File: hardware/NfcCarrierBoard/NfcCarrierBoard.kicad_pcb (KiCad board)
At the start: 2 copper layers, 80 x 100 mm, 50 parts, among them J1 Barrel_Jack, J2 Conn_01x03, J3 JST SH 4, J4 Grove, J5 Conn_01x03, J6 UART, J7 Grove UART, Q1 NMOS, Q2 NMOS, SW1 RESET, U1 24AA02E-OT

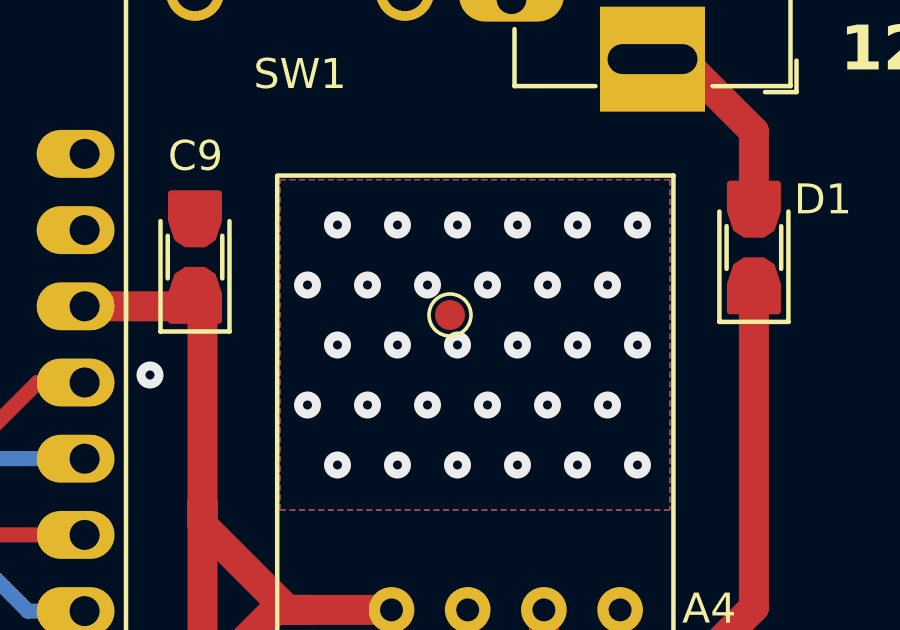
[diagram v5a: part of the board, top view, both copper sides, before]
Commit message: Adjust silkscreen Expose heatsink pad
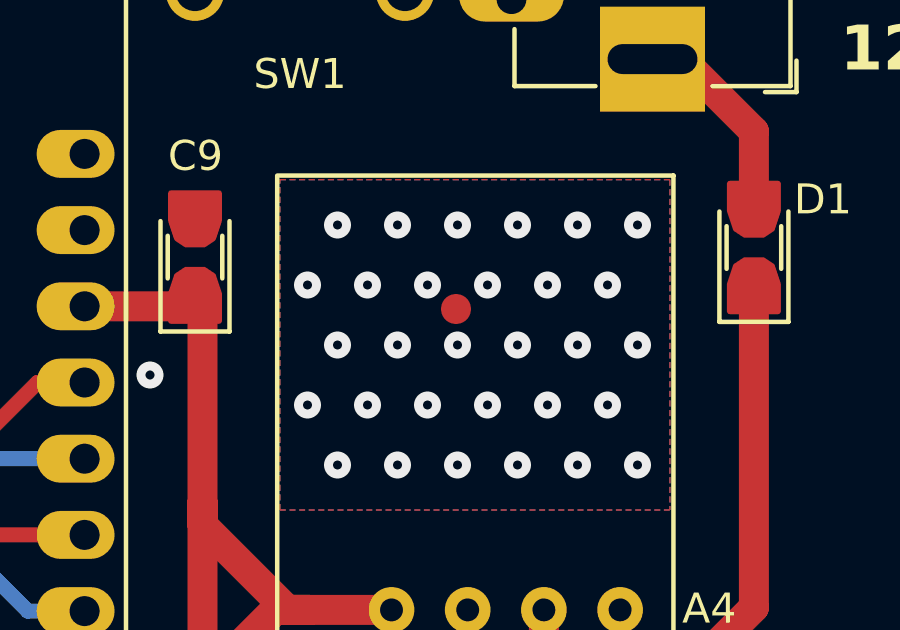
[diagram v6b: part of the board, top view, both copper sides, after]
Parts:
- moved SYM1 2.00 mm to (140.0, 98.0)
- moved HS1 0.28 mm to (160.2, 69.8)
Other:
- board text added: "${PROJECT_URL} Date: ${ISSUE_DATE} Revision: ${REVISION}"
- board text removed: "${PROJECTNAME} Date: ${ISSUE_DATE} Revision: ${REVISION} ${PROJECT_URL}"
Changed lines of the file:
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@@
 		(pad_to_mask_clearance 0)
 		(allow_soldermask_bridges_in_footprints no)
+		(aux_axis_origin 100 150)
 		(pcbplotparams
 			(layerselection 0x00010fc_ffffffff)
@@
 			(outputformat 1)
 			(mirror no)
-			(drillshape 1)
+			(drillshape 0)
 			(scaleselection 1)
-			(outputdirectory "")
+			(outputdirectory "output")
 		)
 	)
@@
 		(locked yes)
 		(layer "F.Cu")
-		(at 160 70)
+		(at 160.2 69.8)
 		(descr "SMD pad as test Point, diameter 1.0mm")
 		(tags "test point SMD pad")
 		(property "Reference" "HS1"
 			(at 0 -1.448 0)
-			(layer "F.SilkS")
+			(layer "F.Fab")
 			(hide yes)
 			(effects
@@
 		(fp_circle
 			(center 0 0)
-			(end 0 0.7)
-			(stroke
-				(width 0.12)
-				(type solid)
-			)
-			(fill none)
-			(layer "F.SilkS")
-		)
-		(fp_circle
-			(center 0 0)
-			(end 1 0)
+			(end 0.73 0.01)
 			(stroke
 				(width 0.05)
@@
 	(footprint "Symbol:OSHW-Logo_19x20mm_SilkScreen"
 		(layer "B.Cu")
-		(at 140 100 180)
+		(at 140 98 180)
 		(descr "Open Source Hardware Logo")
 		(tags "Logo OSHW")
@@
 		)
 	)
+	(gr_rect
+		(start 154.4 65.5)
+		(end 167.3 76.5)
+		(stroke
+			(width 0.1)
+			(type default)
+		)
+		(fill solid)
+		(layer "B.Mask")
+	)
+	(gr_rect
+		(start 154.4 65.5)
+		(end 167.3 76.5)
+		(stroke
+			(width 0.1)
+			(type default)
+		)
+		(fill solid)
+		(layer "F.Mask")
+	)
 	(gr_line
 		(start 100 47)
@@
 		(layer "Edge.Cuts")
 	)
-	(gr_text "${PROJECTNAME}\nDate: ${ISSUE_DATE}\nRevision: ${REVISION}\n${PROJECT_URL}"
-		(at 139.75 118.25 0)
+	(gr_text "${PROJECT_URL}\nDate: ${ISSUE_DATE}\nRevision: ${REVISION}"
+		(at 164 116 0)
 		(layer "B.SilkS")
 		(effects
@@
 				(thickness 0.1875)
 			)
-			(justify top mirror)
+			(justify left top mirror)
 		)
 	)
 	(gr_text "${TITLE}"
-		(at 140 116 0)
+		(at 140 114 0)
 		(layer "B.SilkS")
 		(effects

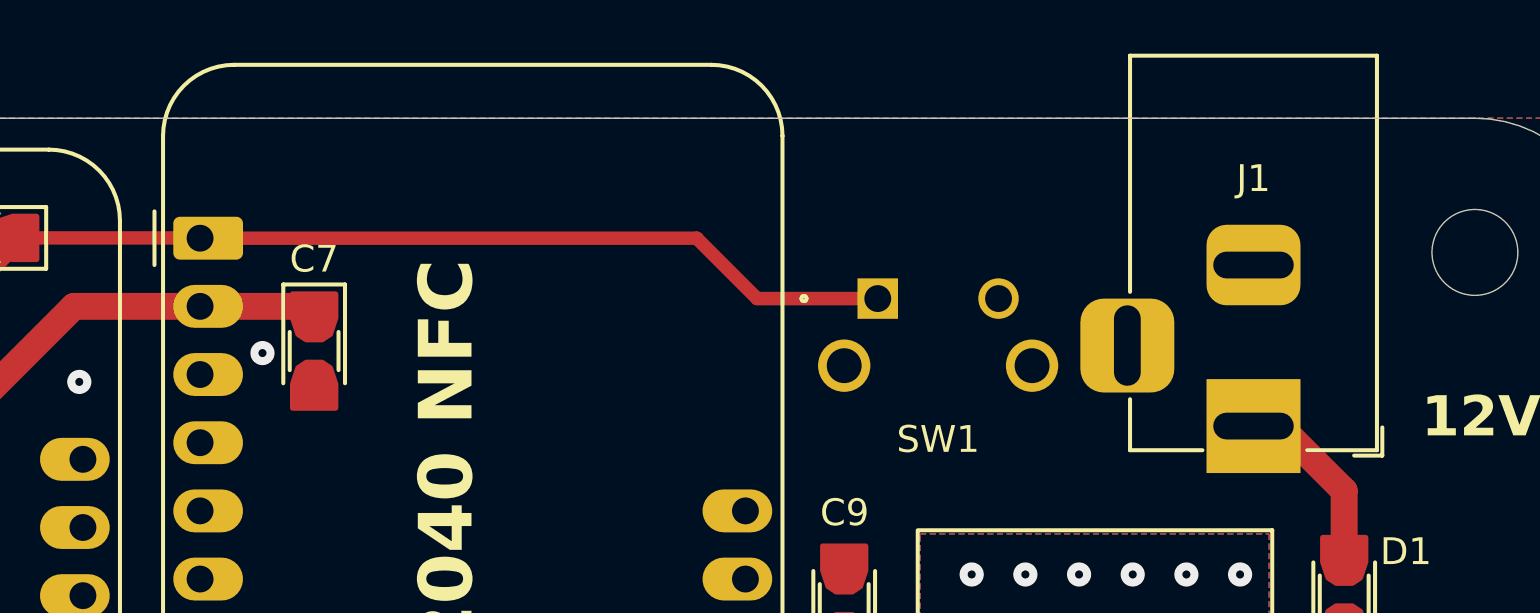
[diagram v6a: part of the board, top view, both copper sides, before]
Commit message: Fix off-board silkscreen
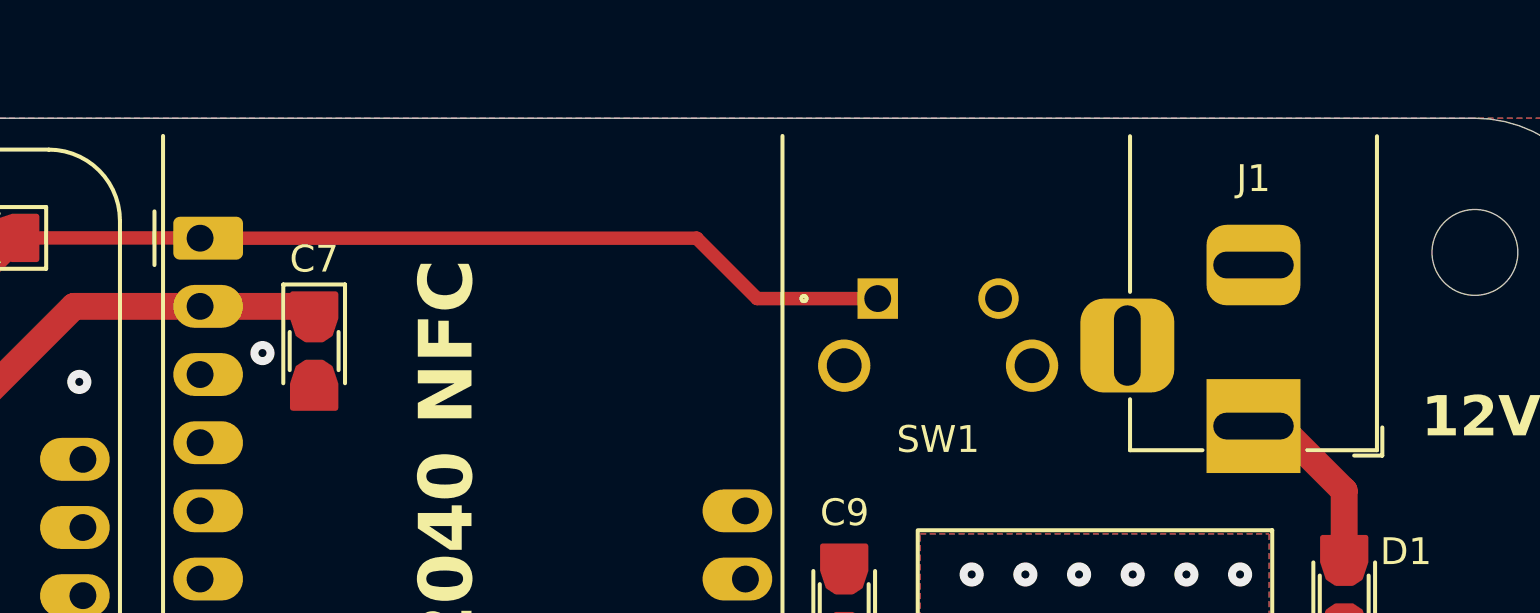
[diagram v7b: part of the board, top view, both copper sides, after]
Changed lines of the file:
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@@
 	)
 	(footprint "Connector_BarrelJack:BarrelJack_Horizontal"
+		(locked yes)
 		(layer "F.Cu")
 		(at 166.75 61.47 -90)
@@
 		(attr through_hole)
 		(fp_line
-			(start -13.8 4.6)
-			(end -13.8 -4.6)
-			(stroke
-				(width 0.15)
-				(type solid)
-			)
-			(layer "F.SilkS")
-		)
-		(fp_line
 			(start -5 4.6)
-			(end -13.8 4.6)
+			(end -10.8 4.6)
 			(stroke
 				(width 0.15)
@@
 		)
 		(fp_line
-			(start -13.8 -4.6)
+			(start -10.8 -4.6)
 			(end 0.9 -4.6)
 			(stroke
@@
 	)
 	(footprint "Module:Adafruit_Feather"
+		(locked yes)
 		(layer "F.Cu")
 		(at 127.5 54.47)
@@
 		)
 		(fp_line
-			(start 19.05 -6.46)
-			(end 1.27 -6.46)
-			(stroke
-				(width 0.15)
-				(type solid)
-			)
-			(layer "F.SilkS")
-		)
-		(fp_line
 			(start 19.05 44.56)
 			(end 1.27 44.56)
@@
 		)
 		(fp_arc
-			(start -1.38 -3.81)
-			(mid -0.603833 -5.683833)
-			(end 1.27 -6.46)
-			(stroke
-				(width 0.15)
-				(type solid)
-			)
-			(layer "F.SilkS")
-		)
-		(fp_arc
 			(start 1.27 44.56)
 			(mid -0.603833 43.783833)
@@
 			(stroke
 				(width 0.15)
-				(type solid)
-			)
-			(layer "F.SilkS")
-		)
-		(fp_arc
-			(start 19.05 -6.46)
-			(mid 20.923833 -5.683833)
-			(end 21.7 -3.81)
-			(stroke
-				(width 0.15)

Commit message: Populate part numbers for BOM
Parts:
- U1: value 24AA02E-OT -> 24AA02E48T
